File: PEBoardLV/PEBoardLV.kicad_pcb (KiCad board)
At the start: 4 copper layers, 113.7 x 78.7 mm, 69 parts, among them J1 BSPD Test Jumper, J10 ECU Debug Connector, J11 SWD Header, J12 Extra Pin Header, J13 CAN Header, J14 UART Header, J15 To TSAL, J2 Beam Interlock, J3 To HV Interlocks, J4 To Left Panel, J5 To Right Panel, J6 To Brake Light, J7 To PE HV, J8 BSPD Reset, J9 Main LV Connector, U1 MCP6004, U10 ISO1050, U11 STM32F405, U2 4072, U3 4071, U4 DE1A1B-L2-12V, U5 74HC595, U6 LM555N, U7 SN754410, U8 NCP1117DT33RKG, U9 L78S05CV-DG, Y1 8MHz

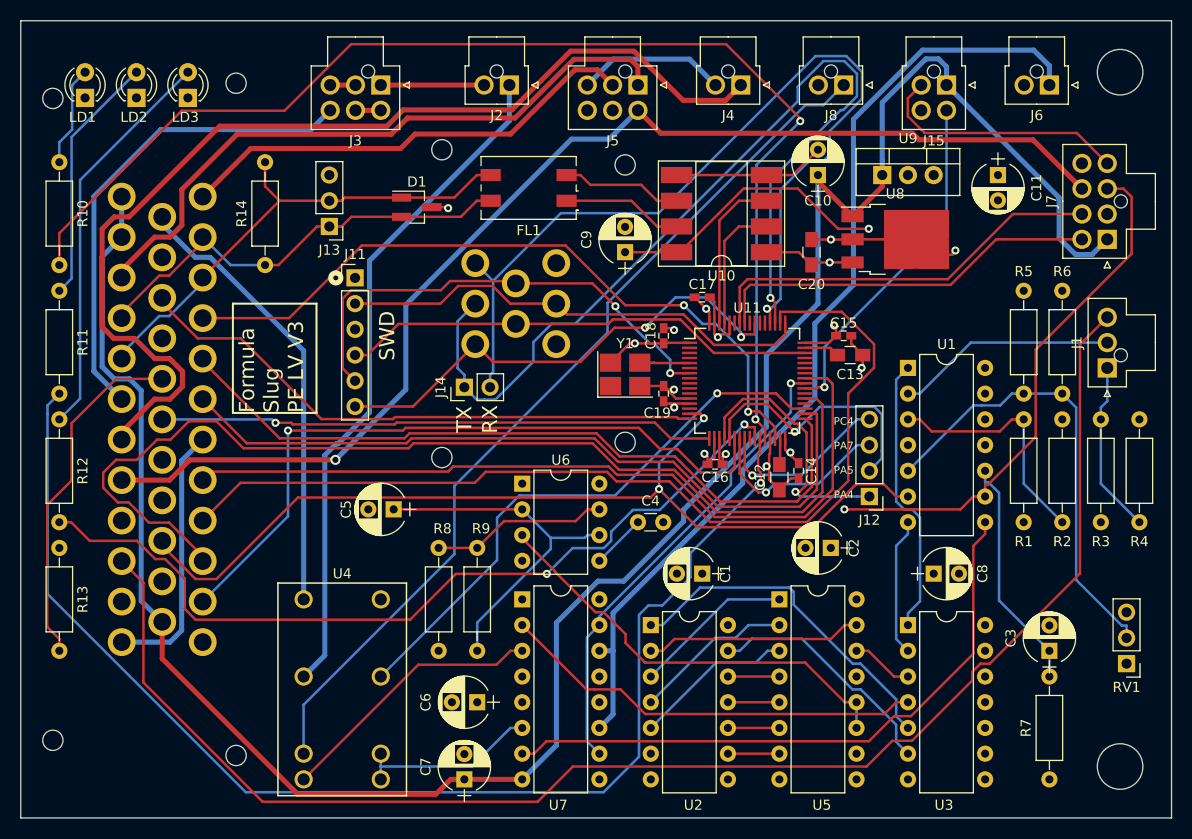
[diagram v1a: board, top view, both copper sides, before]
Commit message: update for sending out second round of PE LV pcb
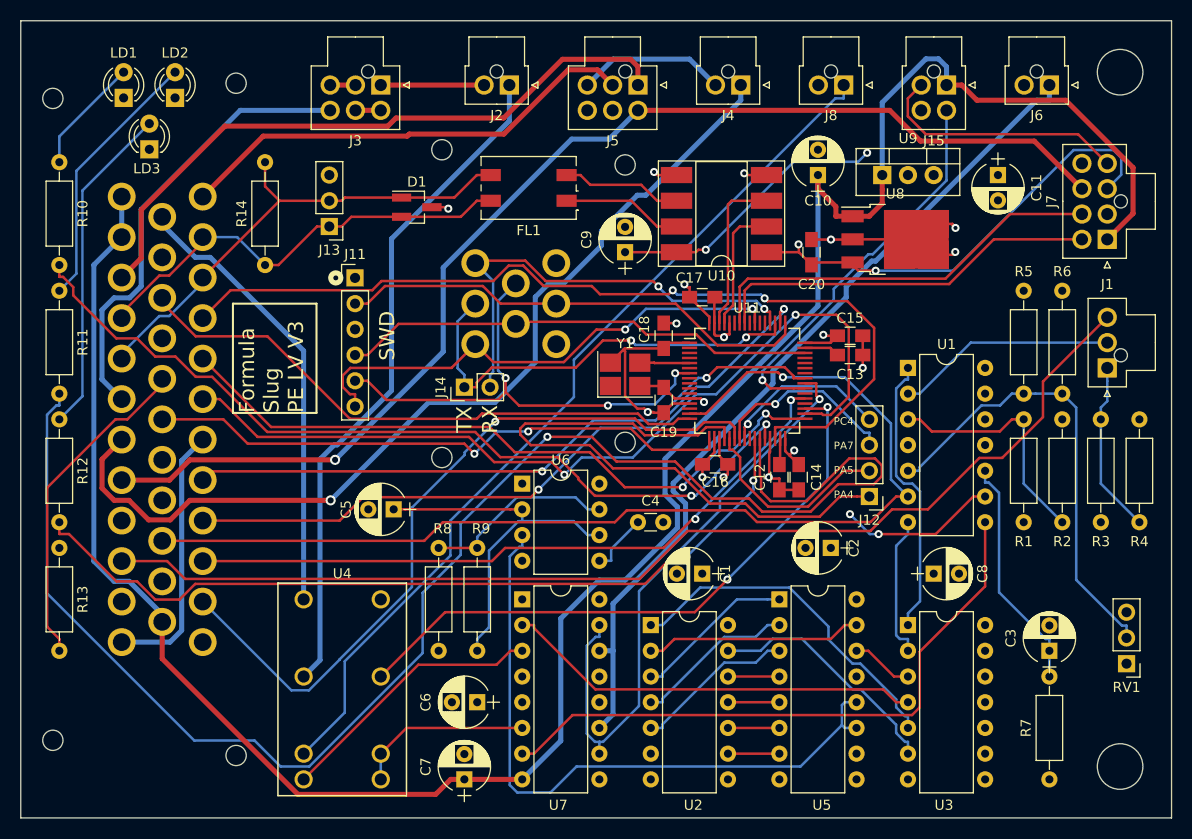
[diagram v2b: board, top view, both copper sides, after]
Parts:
- C14, C15, C16, C17, C18, C19: footprint FSFootprints:C_0402_HandSoldering -> Capacitors_SMD:C_0805_HandSoldering
- moved LD3 6.35 mm to (64.1, 41.9)
- moved LD1 3.81 mm to (61.6, 36.8)
- moved LD2 3.81 mm to (66.7, 36.8)
- moved C14 0.64 mm to (128.3, 74.3)
- moved C15 0.63 mm to (133.3, 60.3)
- moved C19 0.63 mm to (114.9, 66.7)
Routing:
- net /UART_TX: track 93.4 -> 43.8 mm, vias 1 -> 2
- net /UART_RX: track 89.3 -> 45.6 mm, vias 1 -> 2
- net /STATUS_LED_1: track 121.0 -> 85.0 mm
- net /LED_BSPD: track 103.3 -> 67.5 mm, vias 0 -> 2
- net /SIG_CURRENT: track 146.5 -> 110.8 mm
- net /PA4: track 26.3 -> 61.6 mm, vias 1 -> 0
- net /STATUS_LED_2: track 125.7 -> 153.9 mm
- net /LED_IMD: track 95.8 -> 67.8 mm, vias 0 -> 2
- net /CLK: track 43.1 -> 66.3 mm
- net +3V3: track 88.5 -> 109.0 mm, vias 8 -> 9
- net /BUTTON_1: track 71.3 -> 89.3 mm
- net /LED_AMS: track 79.4 -> 64.7 mm, vias 0 -> 2
- net /SIG_BSE: track 93.5 -> 108.0 mm, vias 2 -> 1
- net /SIG_BRAKELT: track 46.8 -> 60.1 mm
- net /BRAKELT_H: track 96.6 -> 85.3 mm
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
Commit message: Update DE relay footprint
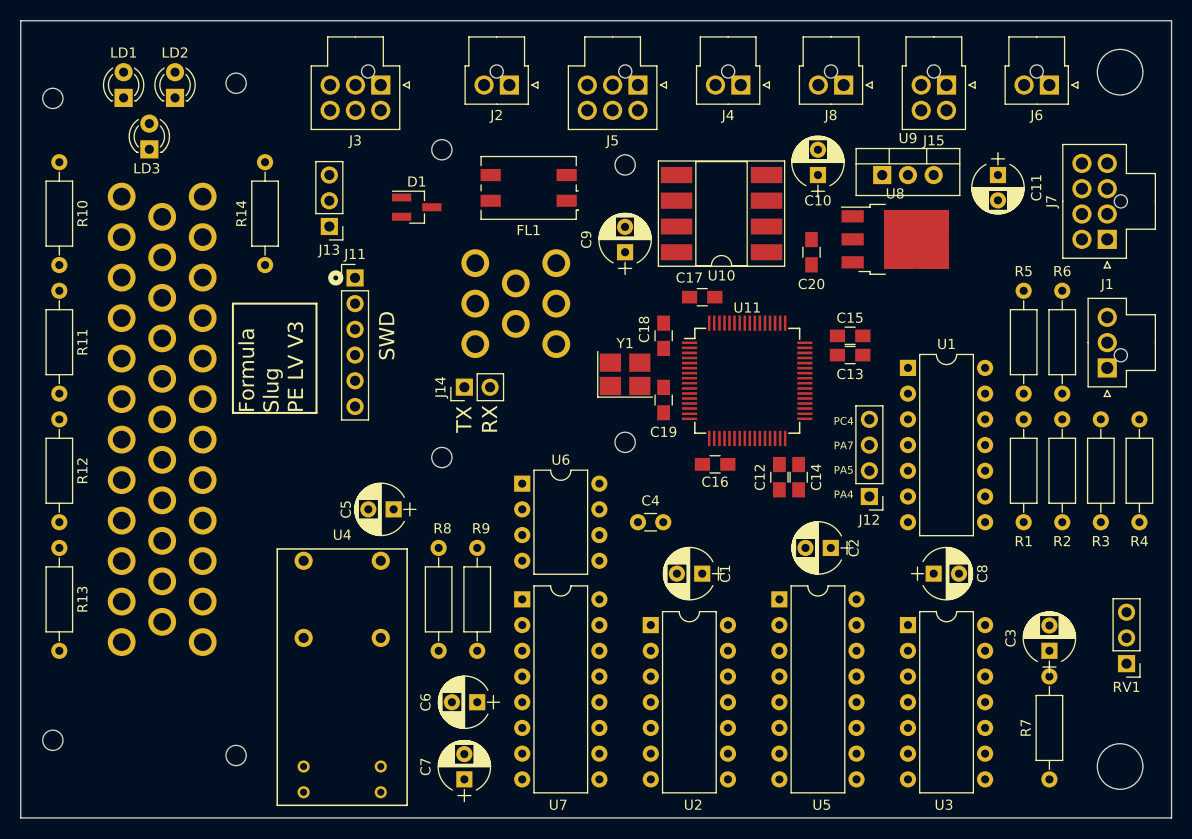
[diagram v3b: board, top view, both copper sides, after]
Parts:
- moved U4 3.81 mm to (87.0, 90.2)
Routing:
- net +12V: track 226.5 -> 0.00 mm
- net /STATUS_LED_2: track 153.9 -> 0.00 mm, vias 1 -> 0
- net /AIRS_FINAL: track 118.0 -> 0.00 mm, vias 1 -> 0
- net /SIG_CURRENT: track 110.8 -> 0.00 mm
- net +3V3: track 109.0 -> 0.00 mm, vias 9 -> 0
- net /SIG_BSE: track 108.0 -> 0.00 mm, vias 1 -> 0
- net /AIRS_ACC_OUT: track 93.3 -> 0.00 mm, vias 1 -> 0
- net /BUTTON_1: track 89.3 -> 0.00 mm, vias 2 -> 0
- net /BSPD_RESET: track 88.6 -> 0.00 mm
- net /BUTTON_3: track 85.9 -> 0.00 mm, vias 2 -> 0
- net /BRAKELT_H: track 85.3 -> 0.00 mm
- net /STATUS_LED_1: track 85.0 -> 0.00 mm, vias 2 -> 0
- net /STATUS_LED_3: track 82.0 -> 0.00 mm, vias 2 -> 0
- net /SIG_STEER: track 74.1 -> 0.00 mm, vias 1 -> 0
- net /BUTTON_2: track 68.3 -> 0.00 mm, vias 2 -> 0
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
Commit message: tweak boards slightly
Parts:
- C1, C2, C6, C7, C8, C9: footprint Capacitors_THT:CP_Radial_D5.0mm_P2.50mm -> Capacitors_THT:C_Disc_D3.0mm_W1.6mm_P2.50mm
- moved J12 18.9 mm to (116.8, 80.6), turned to 90 degrees
- moved C6 15.4 mm to (109.9, 104.1), turned to 90 degrees
- moved R9 13.3 mm to (109.9, 81.3)
- moved C5 6.48 mm to (94.6, 76.2)
- moved C4 3.59 mm to (109.9, 76.2)
- moved U1 2.54 mm to (139.1, 66.0)
- moved U6 2.54 mm to (98.4, 74.9)
- moved U7 2.54 mm to (98.4, 86.4)
- moved R8 1.91 mm to (94.6, 91.4)
- moved C1 1.27 mm to (118.7, 85.1)
- moved C8 1.27 mm to (141.6, 85.1)
- moved C18 1.27 mm to (114.9, 61.6), turned to 270 degrees
- moved C2 1.27 mm to (131.4, 82.5)
- moved C9 1.27 mm to (112.4, 52.1)
- moved U4 1.27 mm to (88.3, 90.2)
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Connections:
- J12 pad 1: /PA4 -> /PA7
- J12 pad 2: /PA5 -> /PC4
- J12 pad 3: /PA7 -> /PC5
- J12 pad 4: /PC4 -> GND
- U11 pad 20: /PA4 -> (no net)
- U11 pad 21: /PA5 -> (no net)
- U11 pad 25: (no net) -> /PC5
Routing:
- net +12V: track 0.00 -> 205.3 mm
- net /SWDIO: track 0.00 -> 189.7 mm
- net /SIG_CURRENT: track 0.00 -> 157.8 mm
- net /AIRS_FINAL: track 0.00 -> 137.0 mm
- net +3V3: track 0.00 -> 128.2 mm, vias 0 -> 6
- net /STATUS_LED_1: track 0.00 -> 123.9 mm, vias 0 -> 2
- net /STATUS_LED_2: track 0.00 -> 120.8 mm, vias 0 -> 1
- net /BRAKELT_H: track 0.00 -> 101.4 mm
- net /SIG_BSE: track 0.00 -> 100.4 mm, vias 0 -> 1
- net /AIRS_ACC_OUT: track 0.00 -> 95.8 mm
- net /BSPD_RESET: track 0.00 -> 89.5 mm
- net /LED_BSPD: track 0.00 -> 89.4 mm
- net GND: track 0.00 -> 88.5 mm, vias 0 -> 5
- net /STATUS_LED_3: track 0.00 -> 88.4 mm
- net /BUTTON_3: track 0.00 -> 83.0 mm, vias 0 -> 1
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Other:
- board text added: "Formula Slug PE LV V3.1"
- board text added: "GND CANL CANH"
- board text added: "GND PC5 PC4 PA7"
- board text removed: "Formula Slug PE LV V3"
- board text removed: "PC4 PA7 PA5 PA4"

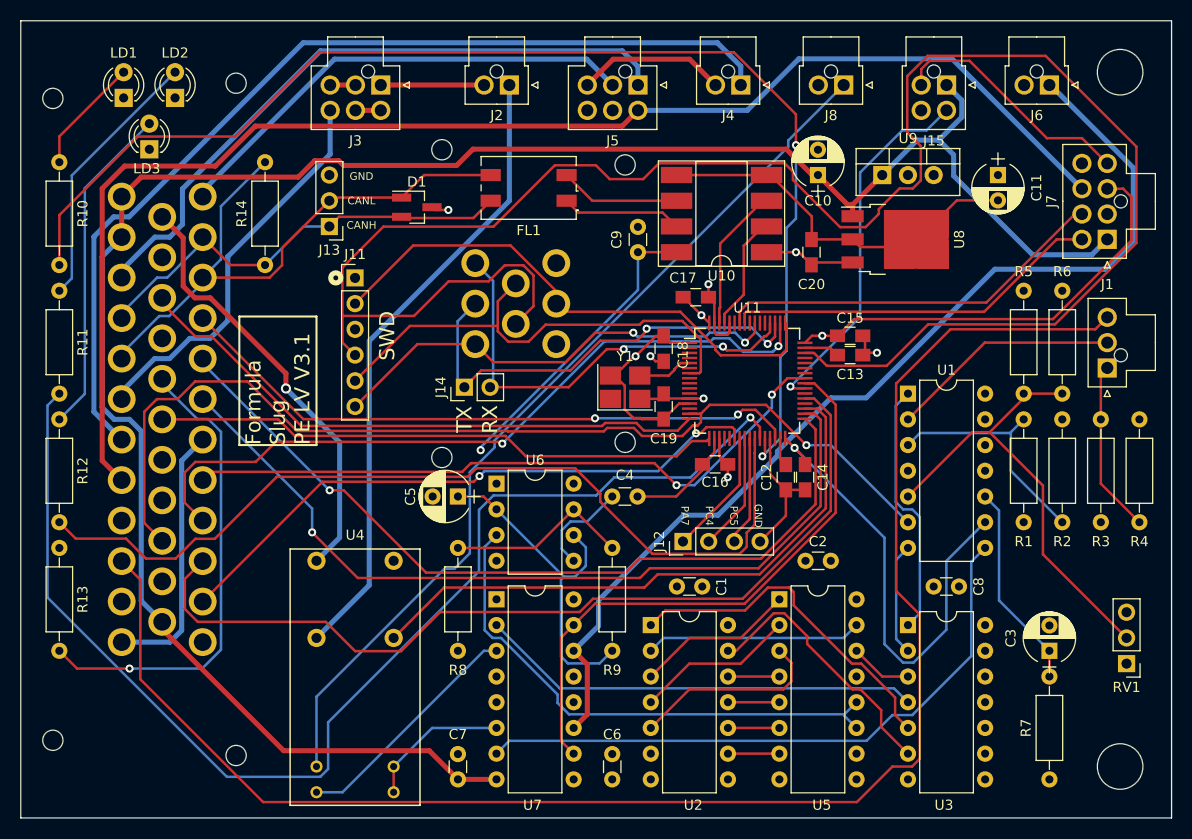
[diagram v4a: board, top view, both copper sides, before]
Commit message: fix 3.3V reg on ECU footprint
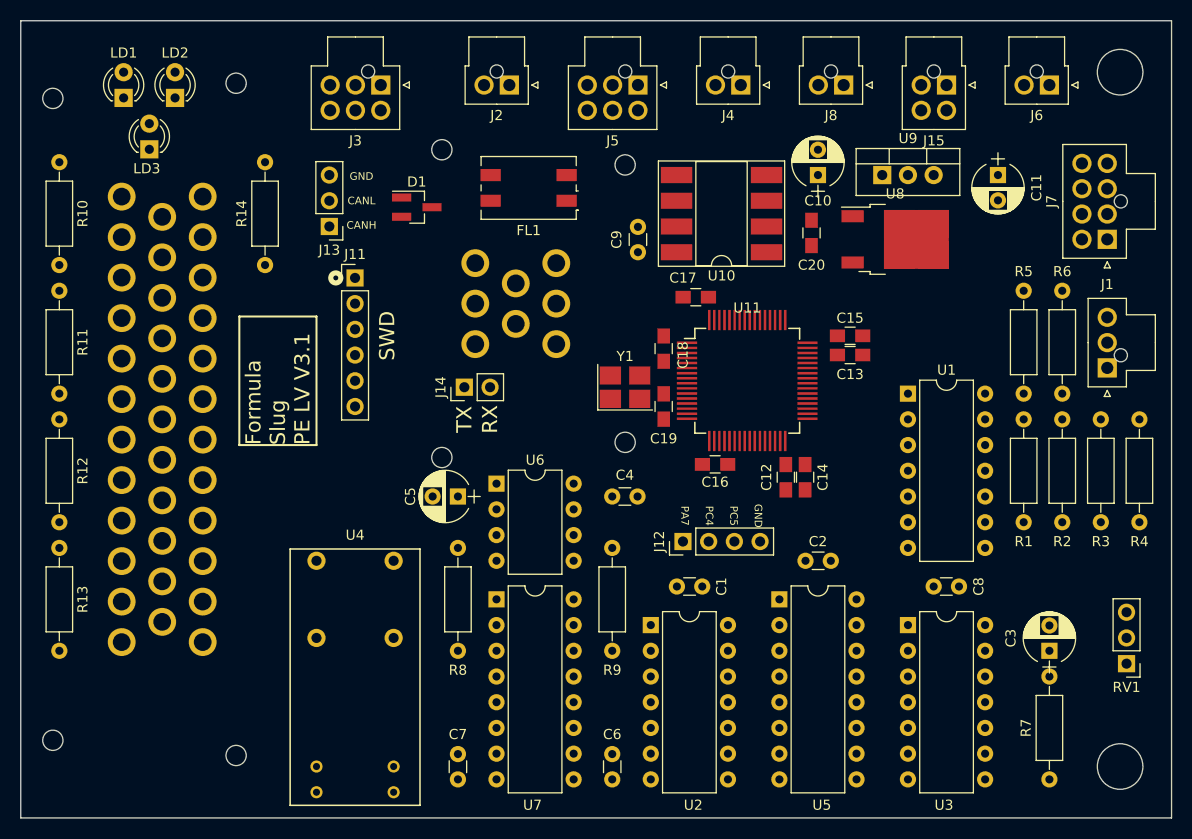
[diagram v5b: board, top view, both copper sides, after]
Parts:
- U8: value NCP1117DT33RKG -> NCP1117-3.3_TO252; footprint TO_SOT_Packages_SMD:TO-252-3_TabPin2 -> TO_SOT_Packages_SMD:TO-252-2
- moved C20 1.91 mm to (129.5, 50.2)
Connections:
- U8 pad 1: +12V -> GND
- U8 pad 2: GND -> +3V3
- U8 pad 3: +3V3 -> +12V
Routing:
- net +12V: track 205.3 -> 0.00 mm
- net /SWDIO: track 189.7 -> 0.00 mm
- net /SIG_CURRENT: track 157.8 -> 0.00 mm
- net /AIRS_FINAL: track 137.0 -> 0.00 mm
- net +3V3: track 128.2 -> 0.00 mm, vias 6 -> 0
- net /STATUS_LED_1: track 123.9 -> 0.00 mm, vias 2 -> 0
- net /STATUS_LED_2: track 120.8 -> 0.00 mm, vias 1 -> 0
- net /BRAKELT_H: track 101.4 -> 0.00 mm
- net /SIG_BSE: track 100.4 -> 0.00 mm, vias 1 -> 0
- net /AIRS_ACC_OUT: track 95.8 -> 0.00 mm
- net /BSPD_RESET: track 89.5 -> 0.00 mm
- net /LED_BSPD: track 89.4 -> 0.00 mm
- net GND: track 88.5 -> 0.00 mm, vias 5 -> 0
- net /STATUS_LED_3: track 88.4 -> 0.00 mm
- net /BUTTON_3: track 83.0 -> 0.00 mm, vias 1 -> 0
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
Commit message: add diodes to relay coils among other things
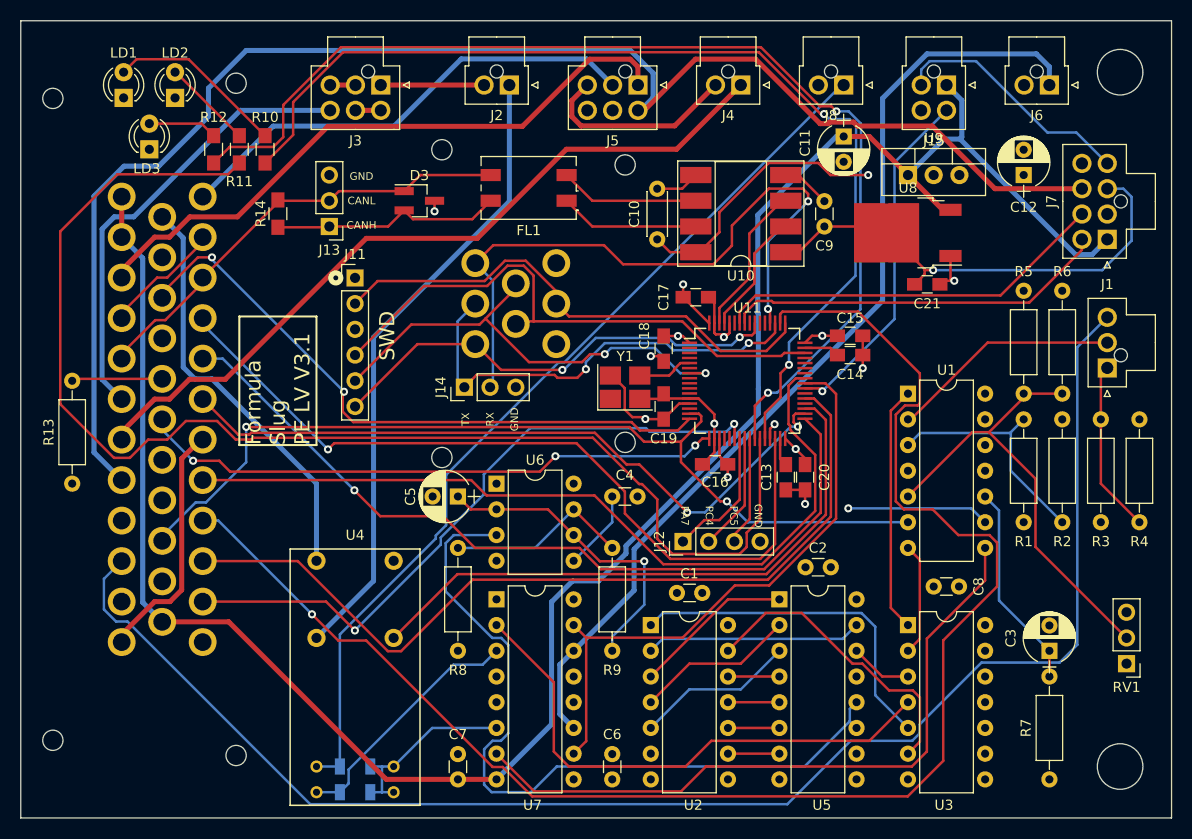
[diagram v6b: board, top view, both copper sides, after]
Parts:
- added C21: 4.7uF, Capacitors_SMD:C_0805_HandSoldering, F.Cu at (141.0, 55.2)
- added D2: D, Diodes_SMD:D_1206, B.Cu at (84.5, 102.9)
- added D3: D_TVS_x2_AAC, TO_SOT_Packages_SMD:SOT-23_Handsoldering, F.Cu at (90.8, 47.0)
- C10: value 10uF -> CP; footprint Capacitors_THT:CP_Radial_D5.0mm_P2.50mm -> Capacitors_THT:C_Disc_D4.3mm_W1.9mm_P5.00mm
- C12: value 2.2uF -> 10uF; footprint Capacitors_SMD:C_0805_HandSoldering -> Capacitors_THT:CP_Radial_D5.0mm_P2.50mm
- C14: value 0.1uF -> 2.2uF
- C20: value 4.7uF -> 0.1uF
- D1: value D_TVS_x2_AAC -> D; footprint TO_SOT_Packages_SMD:SOT-23_Handsoldering -> Diodes_SMD:D_1206; moved to B.Cu
- J14: footprint Pin_Headers:Pin_Header_Straight_1x02_Pitch2.54mm -> Pin_Headers:Pin_Header_Straight_1x03_Pitch2.54mm
- R10, R11, R12, R14: footprint Resistors_THT:R_Axial_DIN0207_L6.3mm_D2.5mm_P10.16mm_Horizontal -> Resistors_SMD:R_0805_HandSoldering
- moved D1 58.1 mm to (84.5, 105.4), turned to 180 degrees
- moved C12 38.0 mm to (150.5, 44.5), turned to 90 degrees
- moved R12 30.7 mm to (70.5, 41.9)
- moved C20 24.1 mm to (128.9, 74.3), turned to 270 degrees
- moved R11 22.6 mm to (73.0, 41.9)
- moved R10 20.4 mm to (75.6, 41.9)
- moved C9 18.6 mm to (130.8, 49.5)
- moved C10 17.1 mm to (114.3, 50.8)
- moved C11 15.7 mm to (132.7, 40.6)
- moved C13 13.6 mm to (127.0, 74.3), turned to 270 degrees
- moved C14 12.9 mm to (133.3, 62.2), turned to 0 degrees
- moved R13 6.48 mm to (56.5, 74.9), turned to 90 degrees
- moved R14 5.24 mm to (76.8, 48.3)
- moved U9 2.54 mm to (139.1, 44.5)
- moved U10 1.91 mm to (122.6, 48.3)
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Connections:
- C10 pad 1: +12V -> +5V
- C11 pad 1: +5V -> +12V
- C12 pad 1: /VCAP_1 -> +5V
- C13 pad 1: /VCAP_2 -> /VCAP_1
- C14 pad 1: +3V3 -> /VCAP_2
- C9 pad 1: +5V -> +3V3
- D1 pad 1: /CAN_L -> /TIMER_H
- D1 pad 2: /CAN_H -> /BSPD_FLT_H
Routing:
- net +12V: track 0.00 -> 208.9 mm
- net /LED_IMD: track 0.00 -> 153.0 mm, vias 0 -> 1
- net /SIG_CURRENT: track 0.00 -> 150.2 mm
- net /AIRS_FINAL: track 0.00 -> 148.8 mm
- net /STATUS_LED_2: track 0.00 -> 128.5 mm
- net /STATUS_LED_3: track 0.00 -> 109.6 mm, vias 0 -> 2
- net /STATUS_LED_1: track 0.00 -> 102.4 mm, vias 0 -> 2
- net /BRAKELT_H: track 0.00 -> 96.6 mm
- net +3V3: track 0.00 -> 96.5 mm, vias 0 -> 8
- net /BSPD_RESET: track 0.00 -> 90.7 mm
- net /SIG_BSE: track 0.00 -> 90.4 mm, vias 0 -> 2
- net /LED_BSPD: track 0.00 -> 84.5 mm
- net /BUTTON_2: track 0.00 -> 81.9 mm, vias 0 -> 1
- net /LED_AMS: track 0.00 -> 81.5 mm
- net /BUTTON_1: track 0.00 -> 79.5 mm, vias 0 -> 1
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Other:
- board text added: "TX RX GND"
- board text removed: "RX"
- board text removed: "TX"

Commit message: hopefully finalize PCBs for send to manufacturing
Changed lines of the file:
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@@
   (layers
     (0 F.Cu signal)
-    (1 In1.Cu power)
+    (1 In1.Cu power hide)
     (2 In2.Cu power hide)
     (31 B.Cu signal)
@@
     (descr "TO-220-3, Vertical, RM 2.54mm")
     (tags "TO-220-3 Vertical RM 2.54mm")
-    (fp_text reference U9 (at 2.54 -3.62) (layer F.SilkS)
+    (fp_text reference U9 (at 6.985 3.175) (layer F.SilkS)
       (effects (font (size 1 1) (thickness 0.15)))
     )
@@
     (tags "DPAK TO-252 DPAK-3 TO-252-3 SOT-428")
     (attr smd)
-    (fp_text reference U8 (at 0 4.445 180) (layer F.SilkS)
+    (fp_text reference U8 (at 2.54 -4.445 180) (layer F.SilkS)
       (effects (font (size 1 1) (thickness 0.15)))
     )
@@
     (effects (font (size 1.5 1.5) (thickness 0.3)))
   )
-  (segment (start 150.495 44.45) (end 152.273 44.45) (width 0.25) (layer In1.Cu) (net 1) (status 400000))
-  (segment (start 159.933 48.3) (end 158.75 48.3) (width 0.25) (layer In1.Cu) (net 1) (status 800000))
+  (segment (start 150.495 44.45) (end 152.273 44.45) (width 0.25) (layer In1.Cu) (net 1))
+  (segment (start 159.933 48.3) (end 158.75 48.3) (width 0.25) (layer In1.Cu) (net 1))
   (segment (start 162.306 50.673) (end 159.933 48.3) (width 0.25) (layer In1.Cu) (net 1))
   (segment (start 162.306 41.148) (end 162.306 50.673) (width 0.25) (layer In1.Cu) (net 1))
@@
   (segment (start 118.4684 52.07) (end 120.44 50.0984) (width 0.25) (layer F.Cu) (net 1))
   (segment (start 118.11 52.07) (end 118.4684 52.07) (width 0.25) (layer F.Cu) (net 1))
-  (segment (start 127 44.45) (end 128.23 44.45) (width 0.25) (layer F.Cu) (net 2) (status C00000))
-  (segment (start 128.23 44.45) (end 130.81 47.03) (width 0.25) (layer F.Cu) (net 2) (status C00000))
+  (segment (start 127 44.45) (end 128.23 44.45) (width 0.25) (layer F.Cu) (net 2))
+  (segment (start 128.23 44.45) (end 130.81 47.03) (width 0.25) (layer F.Cu) (net 2))
   (segment (start 127.0533 44.5033) (end 127 44.45) (width 0.25) (layer F.Cu) (net 2))
   (via (at 125.8938 69.0573) (size 0.8) (layers F.Cu B.Cu) (net 2))
@@
   (segment (start 131.39 61.52) (end 132.1 62.23) (width 0.25) (layer F.Cu) (net 8))
   (segment (start 128.89 61.52) (end 131.39 61.52) (width 0.25) (layer F.Cu) (net 8))
-  (segment (start 127 52.07) (end 128.27 52.07) (width 0.25) (layer F.Cu) (net 9) (status C00000))
-  (segment (start 128.27 52.07) (end 130.81 49.53) (width 0.25) (layer F.Cu) (net 9) (status C00000))
+  (segment (start 127 52.07) (end 128.27 52.07) (width 0.25) (layer F.Cu) (net 9))
+  (segment (start 128.27 52.07) (end 130.81 49.53) (width 0.25) (layer F.Cu) (net 9))
   (via (at 130.6065 60.325) (size 0.8) (layers F.Cu B.Cu) (net 9))
   (via (at 116.86 55.2474) (size 0.8) (layers F.Cu B.Cu) (net 9))
